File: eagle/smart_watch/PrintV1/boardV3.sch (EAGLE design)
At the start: 62 parts, among them U1 MCP73831, U2 TPS61200, U3 MAX1704X, U4 V_REG_LDOSMD, Y1 16MHz

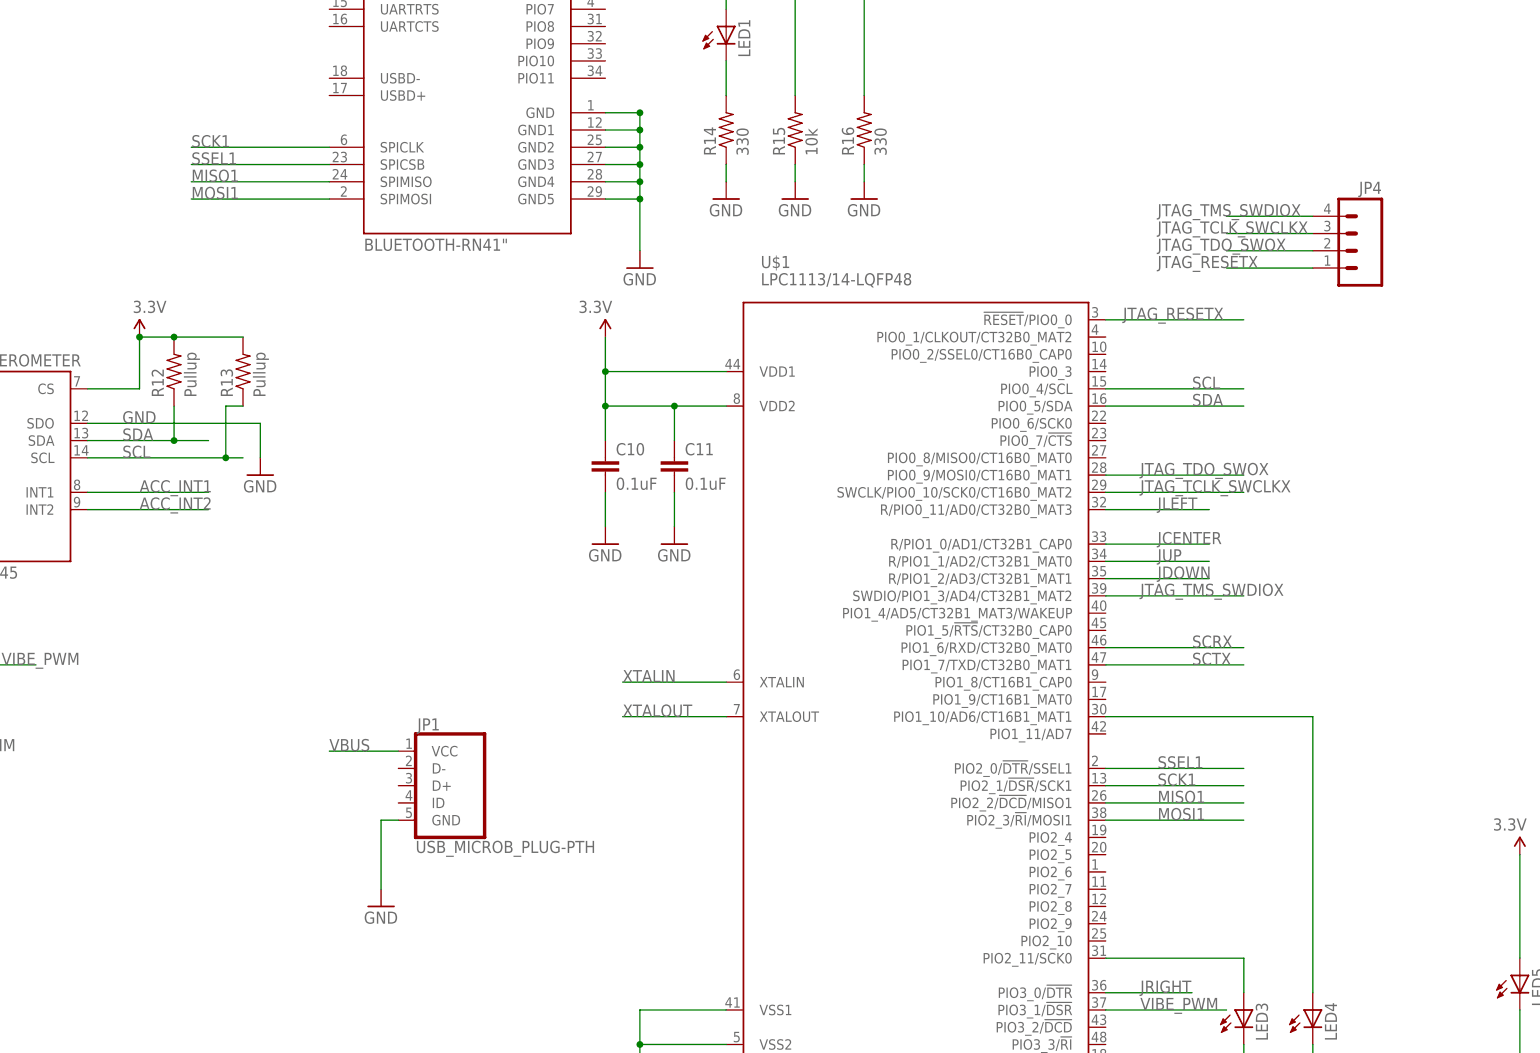
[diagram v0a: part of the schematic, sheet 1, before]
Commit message: Fixed up git ignore for xpress;
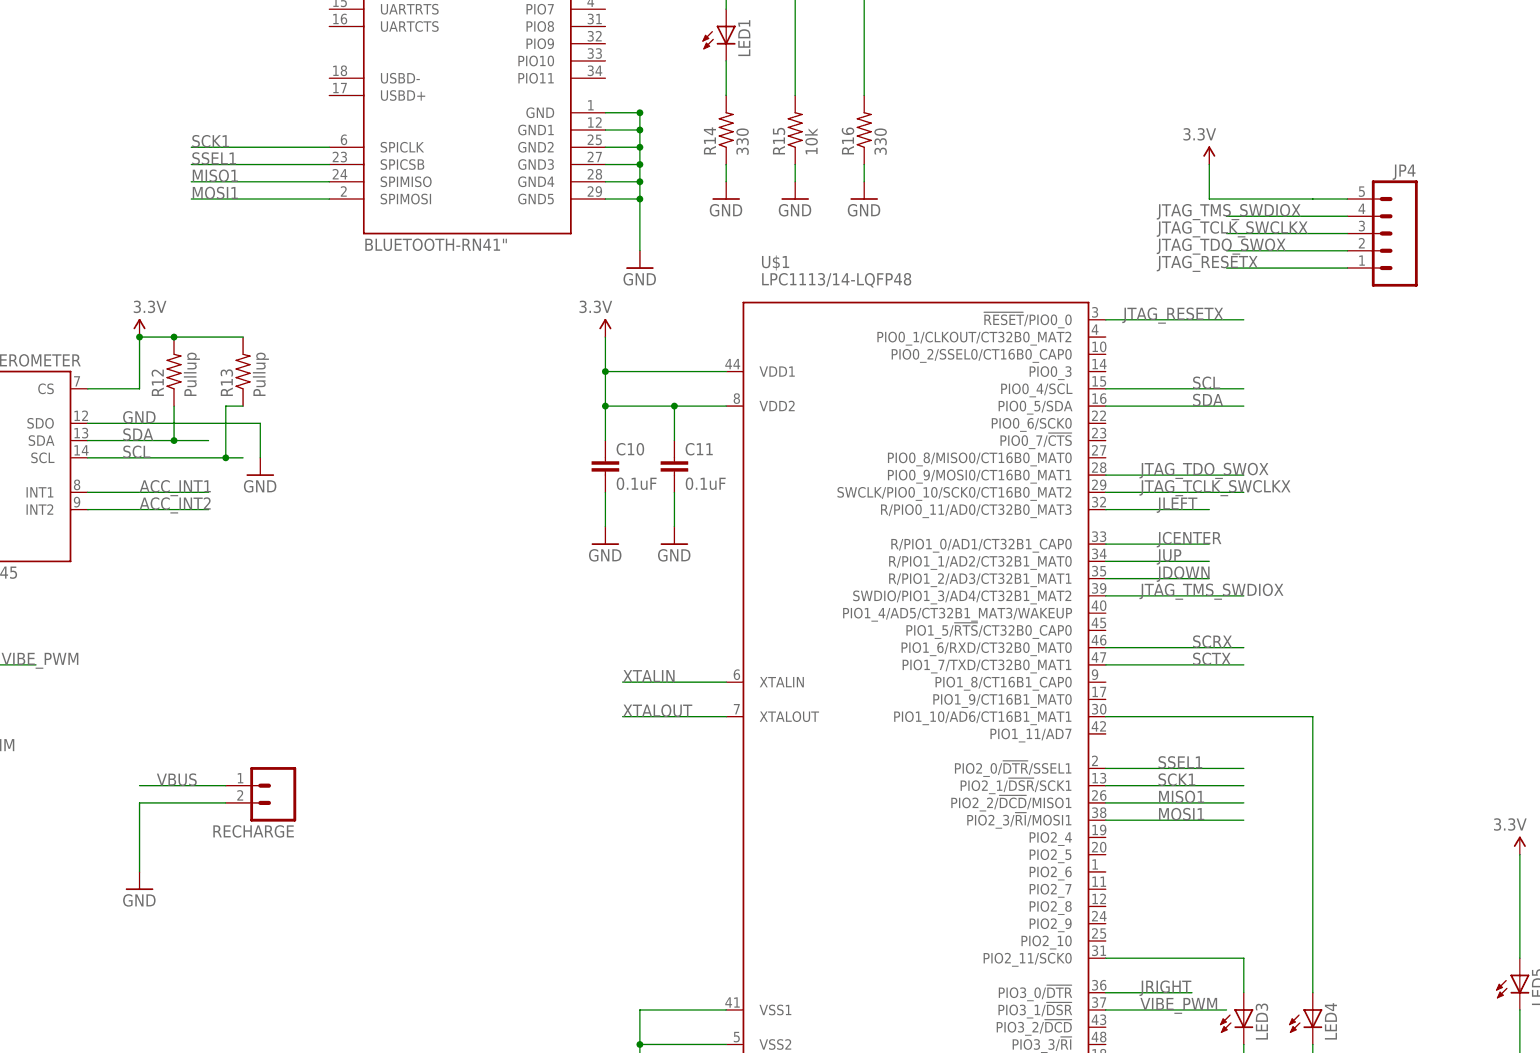
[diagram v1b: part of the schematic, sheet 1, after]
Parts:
- removed JP1: USB_MICROB_PLUG-PTH, SparkFun-Connectors:USB_MICROB_PLUG-PTH
- added RECHARGE: (no value), SparkFun-Connectors:M02POLAR
- I2C: device SparkFun-Connectors:M02POGO_PIN_HOLES_ONLY -> SparkFun-Connectors:M02POLAR
- JP2: device SparkFun-Connectors:M02-JST-2-PTH-NO_SILK -> SparkFun-Connectors:M02PTH
- JP4: device SparkFun-Connectors:M04POLAR -> SparkFun-Connectors:M05PTH
- R12, R13: device SparkFun-Passives:RESISTOR0402-RES -> SparkFun-Resistors:RESISTOR0603-RES
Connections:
- net 3.3V: now also JP4.5
- net GND: now also RECHARGE.2; no longer JP1.GND
- net VBUS: now also RECHARGE.1; no longer JP1.VCC
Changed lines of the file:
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@@
 <?xml version="1.0" encoding="utf-8"?>
 <!DOCTYPE eagle SYSTEM "eagle.dtd">
-<eagle version="6.2">
+<eagle version="6.4">
 <drawing>
 <settings>
@@
 <parts>
 <part name="U$1" library="lpc1100v1.1" deviceset="LPC1113/14-LQFP48" device=""/>
-<part name="JP1" library="SparkFun-Connectors" deviceset="USB_MICROB_PLUG" device="-PTH"/>
 <part name="U1" library="SparkFun-PowerIC" deviceset="MCP73831" device=""/>
-<part name="JP2" library="SparkFun-Connectors" deviceset="M02" device="-JST-2-PTH-NO_SILK"/>
-<part name="GND1" library="SparkFun-Aesthetics" deviceset="GND" device=""/>
+<part name="JP2" library="SparkFun-Connectors" deviceset="M02" device="PTH"/>
 <part name="C1" library="SparkFun-Passives" deviceset="CAP" device="0603-CAP" value="4.7uF"/>
 <part name="GND2" library="SparkFun-Aesthetics" deviceset="GND" device=""/>
@@
 <part name="SUPPLY7" library="SparkFun-Aesthetics" deviceset="3.3V" device=""/>
 <part name="GND23" library="SparkFun-Aesthetics" deviceset="GND" device=""/>
-<part name="JP4" library="SparkFun-Connectors" deviceset="M04" device="POLAR"/>
+<part name="JP4" library="SparkFun-Connectors" deviceset="M05" device="PTH"/>
 <part name="C10" library="SparkFun-Passives" deviceset="CAP" device="0603-CAP" value="0.1uF"/>
 <part name="C11" library="SparkFun-Passives" deviceset="CAP" device="0603-CAP" value="0.1uF"/>
@@
 <part name="GND29" library="SparkFun-Aesthetics" deviceset="GND" device=""/>
 <part name="SUPPLY8" library="SparkFun-Aesthetics" deviceset="3.3V" device=""/>
-<part name="R12" library="SparkFun-Passives" deviceset="RESISTOR" device="0402-RES" value="Pullup"/>
-<part name="R13" library="SparkFun-Passives" deviceset="RESISTOR" device="0402-RES" value="Pullup"/>
+<part name="R12" library="SparkFun-Resistors" deviceset="RESISTOR" device="0603-RES" value="Pullup"/>
+<part name="R13" library="SparkFun-Resistors" deviceset="RESISTOR" device="0603-RES" value="Pullup"/>
 <part name="Y1" library="SparkFun-FreqCtrl" deviceset="CRYSTAL" device="5X3" value="16MHz"/>
 <part name="C12" library="SparkFun-Passives" deviceset="CAP" device="0603-CAP" value="16pF"/>
@@
 <part name="SUPPLY11" library="SparkFun-Aesthetics" deviceset="3.3V" device=""/>
 <part name="SPI" library="SparkFun-Connectors" deviceset="M04" device="POLAR"/>
-<part name="I2C" library="SparkFun-Connectors" deviceset="M02" device="POGO_PIN_HOLES_ONLY"/>
+<part name="I2C" library="SparkFun-Connectors" deviceset="M02" device="POLAR"/>
 <part name="LED5" library="SparkFun-LED" deviceset="LED" device="0603"/>
 <part name="R23" library="SparkFun-Passives" deviceset="RESISTOR" device="0603-RES" value="330"/>
 <part name="GND39" library="SparkFun-Aesthetics" deviceset="GND" device=""/>
 <part name="SUPPLY12" library="SparkFun-Aesthetics" deviceset="3.3V" device=""/>
+<part name="RECHARGE" library="SparkFun-Connectors" deviceset="M02" device="POLAR"/>
+<part name="GND40" library="SparkFun-Aesthetics" deviceset="GND" device=""/>
+<part name="SUPPLY13" library="SparkFun-Aesthetics" deviceset="3.3V" device=""/>
 </parts>
 <sheets>
@@
 <instances>
 <instance part="U$1" gate="LPC" x="264.16" y="63.5"/>
-<instance part="JP1" gate="G$1" x="195.58" y="50.8"/>
 <instance part="U1" gate="G$1" x="-12.7" y="58.42" rot="MR0"/>
 <instance part="JP2" gate="G$1" x="-88.9" y="58.42"/>
-<instance part="GND1" gate="1" x="185.42" y="33.02"/>
 <instance part="C1" gate="G$1" x="43.18" y="55.88"/>
 <instance part="GND2" gate="1" x="43.18" y="43.18"/>
@@
 <instance part="SUPPLY7" gate="G$1" x="114.3" y="116.84"/>
 <instance part="GND23" gate="1" x="111.76" y="76.2"/>
-<instance part="JP4" gate="G$1" x="327.66" y="129.54" rot="MR0"/>
+<instance part="JP4" gate="G$1" x="335.28" y="132.08" rot="MR0"/>
 <instance part="C10" gate="G$1" x="218.44" y="96.52"/>
 <instance part="C11" gate="G$1" x="228.6" y="96.52"/>
@@
 <instance part="GND39" gate="1" x="353.06" y="-7.62"/>
 <instance part="SUPPLY12" gate="G$1" x="353.06" y="40.64" rot="MR0"/>
+<instance part="RECHARGE" gate="G$1" x="170.18" y="50.8" rot="R180"/>
+<instance part="GND40" gate="1" x="149.86" y="35.56"/>
+<instance part="SUPPLY13" gate="G$1" x="307.34" y="142.24" rot="MR0"/>
 </instances>
 <busses>
@@
 <nets>
 <net name="GND" class="0">
-<segment>
-<pinref part="JP1" gate="G$1" pin="GND"/>
-<pinref part="GND1" gate="1" pin="GND"/>
-<wire x1="187.96" y1="45.72" x2="185.42" y2="45.72" width="0.1524" layer="91"/>
-<wire x1="185.42" y1="45.72" x2="185.42" y2="35.56" width="0.1524" layer="91"/>
-</segment>
 <segment>
 <pinref part="C1" gate="G$1" pin="2"/>
@@
 <pinref part="R23" gate="G$1" pin="1"/>
 <pinref part="GND39" gate="1" pin="GND"/>
+</segment>
+<segment>
+<pinref part="RECHARGE" gate="G$1" pin="2"/>
+<wire x1="162.56" y1="48.26" x2="149.86" y2="48.26" width="0.1524" layer="91"/>
+<wire x1="149.86" y1="48.26" x2="149.86" y2="38.1" width="0.1524" layer="91"/>
+<pinref part="GND40" gate="1" pin="GND"/>
 </segment>
 </net>
@@
 <pinref part="SUPPLY12" gate="G$1" pin="3.3V"/>
 </segment>
+<segment>
+<pinref part="JP4" gate="G$1" pin="5"/>
+<wire x1="327.66" y1="137.16" x2="322.58" y2="137.16" width="0.2032" layer="91"/>
+<wire x1="322.58" y1="137.16" x2="307.34" y2="137.16" width="0.1524" layer="91"/>
+<wire x1="307.34" y1="137.16" x2="307.34" y2="142.24" width="0.1524" layer="91"/>
+<pinref part="SUPPLY13" gate="G$1" pin="3.3V"/>
+</segment>
 </net>
 <net name="SCIO2" class="0">
@@
 <segment>
 <pinref part="JP4" gate="G$1" pin="4"/>
-<wire x1="322.58" y1="134.62" x2="309.88" y2="134.62" width="0.2032" layer="91"/>
+<wire x1="327.66" y1="134.62" x2="309.88" y2="134.62" width="0.2032" layer="91"/>
 <label x="299.72" y="134.62" size="1.778" layer="95"/>
 </segment>
@@
 <segment>
 <pinref part="JP4" gate="G$1" pin="3"/>
-<wire x1="322.58" y1="132.08" x2="309.88" y2="132.08" width="0.2032" layer="91"/>
+<wire x1="327.66" y1="132.08" x2="309.88" y2="132.08" width="0.2032" layer="91"/>
 <label x="299.72" y="132.08" size="1.778" layer="95"/>
 </segment>
@@
 <segment>
 <pinref part="JP4" gate="G$1" pin="2"/>
-<wire x1="322.58" y1="129.54" x2="309.88" y2="129.54" width="0.2032" layer="91"/>
+<wire x1="327.66" y1="129.54" x2="309.88" y2="129.54" width="0.2032" layer="91"/>
 <label x="299.72" y="129.54" size="1.778" layer="95"/>
 </segment>
@@
 <segment>
 <pinref part="JP4" gate="G$1" pin="1"/>
-<wire x1="322.58" y1="127" x2="309.88" y2="127" width="0.2032" layer="91"/>
+<wire x1="327.66" y1="127" x2="309.88" y2="127" width="0.2032" layer="91"/>
 <label x="299.72" y="127" size="1.778" layer="95"/>
 </segment>
@@
 </segment>
 <segment>
-<pinref part="JP1" gate="G$1" pin="VCC"/>
-<wire x1="187.96" y1="55.88" x2="177.8" y2="55.88" width="0.2032" layer="91"/>
-<label x="177.8" y="55.88" size="1.778" layer="95"/>
-</segment>
-</net>
+<pinref part="RECHARGE" gate="G$1" pin="1"/>
+<wire x1="162.56" y1="50.8" x2="149.86" y2="50.8" width="0.1524" layer="91"/>
+<label x="152.4" y="50.8" size="1.778" layer="95"/>
+</segment>
+</net>
